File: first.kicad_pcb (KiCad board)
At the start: 2 copper layers, 100 x 100 mm, 52 parts, among them J1 Conn_01x02_Socket, J10 Conn_01x02_Socket, J11 USB_C_Receptacle_USB2.0_16P, J12 Conn_01x03_Socket, J2 Conn_01x03_Socket, J3 Conn_01x03_Socket, J4 Conn_01x03_Socket, J5 Conn_01x03_Socket, J6 Conn_01x03_Socket, J7 Conn_01x03_Socket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

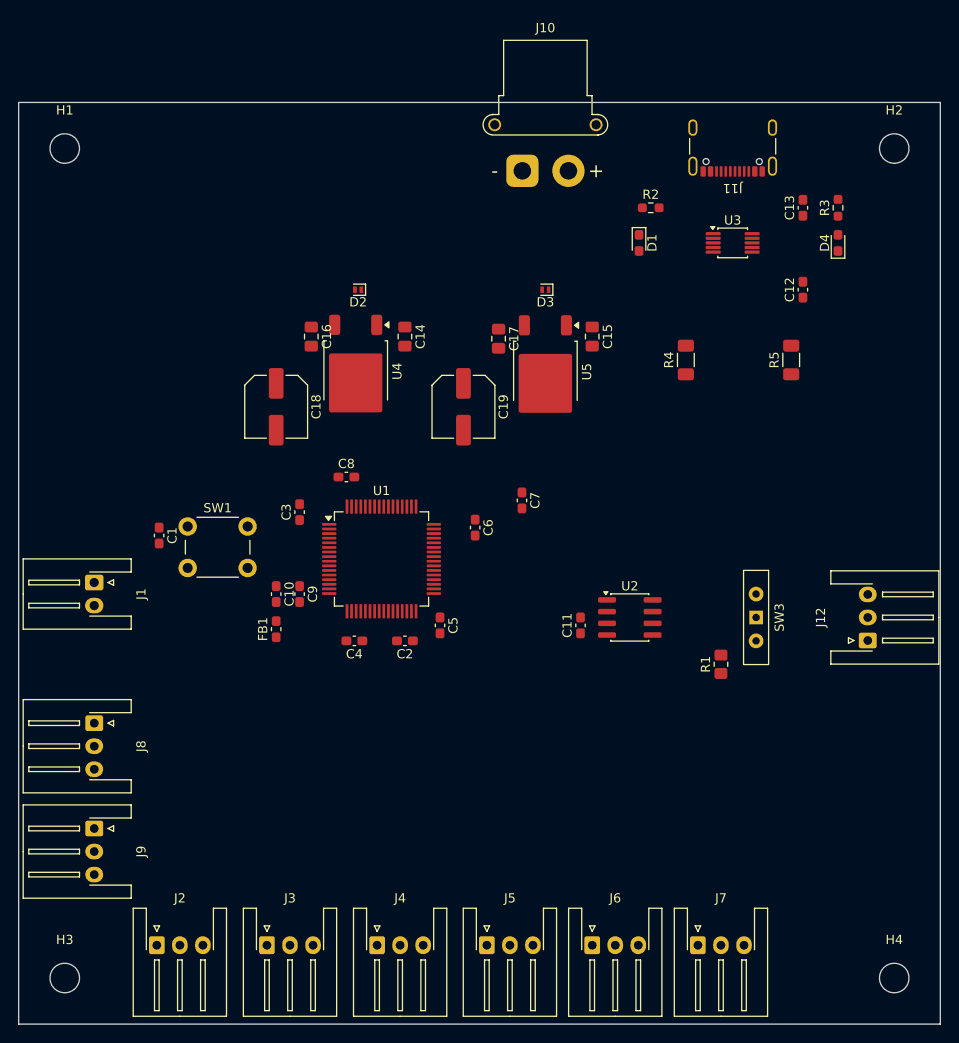
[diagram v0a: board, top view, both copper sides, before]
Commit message: Add files via upload
フリールーティングの実験を行った
電源回りの配線は手動で行う必要あり
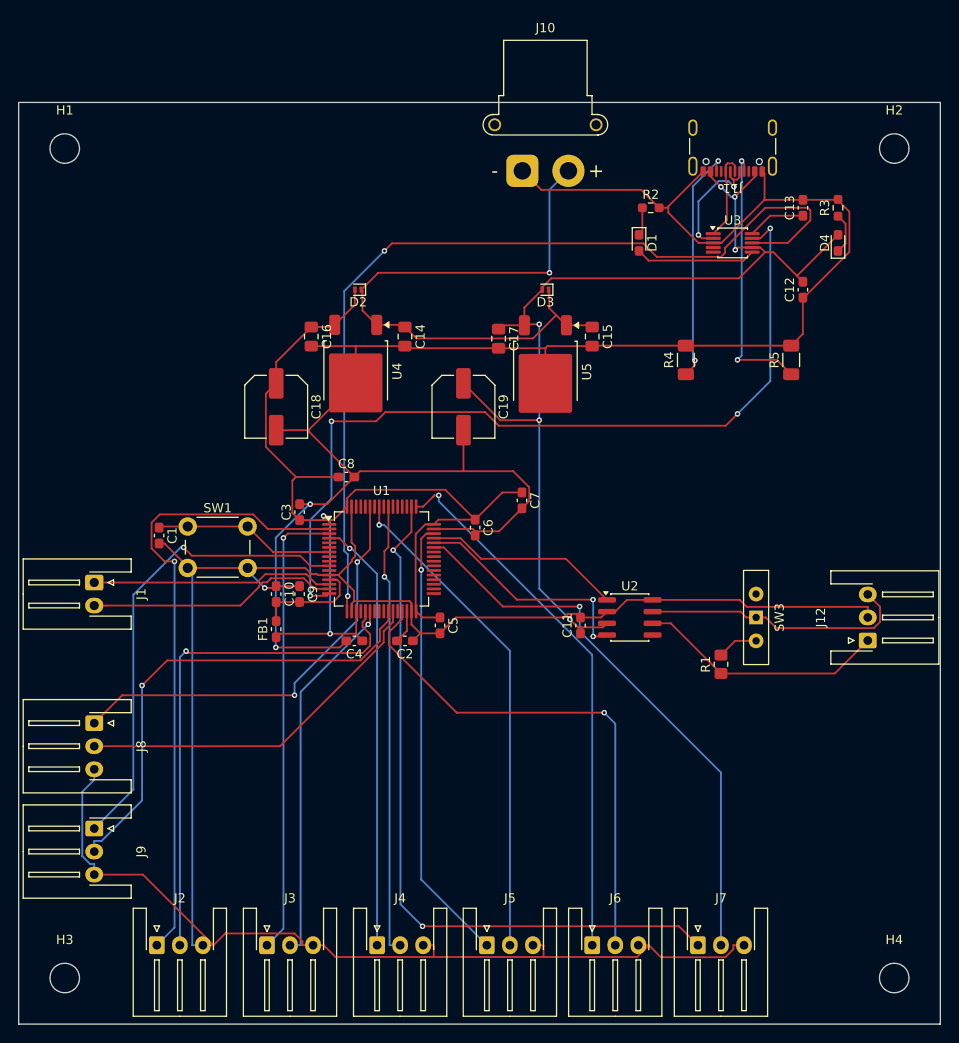
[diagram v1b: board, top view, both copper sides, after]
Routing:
- net GND: track 0.00 -> 460.5 mm, vias 0 -> 3
- net +5V: track 0.00 -> 112.6 mm, vias 0 -> 6
- net +3.3V: track 0.00 -> 110.1 mm, vias 0 -> 2
- net UARTrx: track 0.00 -> 99.3 mm, vias 0 -> 2
- net UARTtx: track 0.00 -> 91.7 mm, vias 0 -> 4
- net m6d: track 0.00 -> 78.4 mm, vias 0 -> 2
- net m1d: track 0.00 -> 68.6 mm, vias 0 -> 1
- net VCC: track 0.00 -> 66.3 mm, vias 0 -> 1
- net m6: track 0.00 -> 61.6 mm, vias 0 -> 1
- net m5d: track 0.00 -> 58.9 mm, vias 0 -> 1
- net m1: track 0.00 -> 56.8 mm, vias 0 -> 1
- net m5: track 0.00 -> 56.4 mm, vias 0 -> 1
- net m4: track 0.00 -> 53.8 mm, vias 0 -> 1
- net m8: track 0.00 -> 52.1 mm, vias 0 -> 1
- net m8d: track 0.00 -> 51.3 mm, vias 0 -> 1
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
